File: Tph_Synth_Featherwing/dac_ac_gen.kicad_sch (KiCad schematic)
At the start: 11 parts, among them J3 Conn_01x04, U4 MCP4728

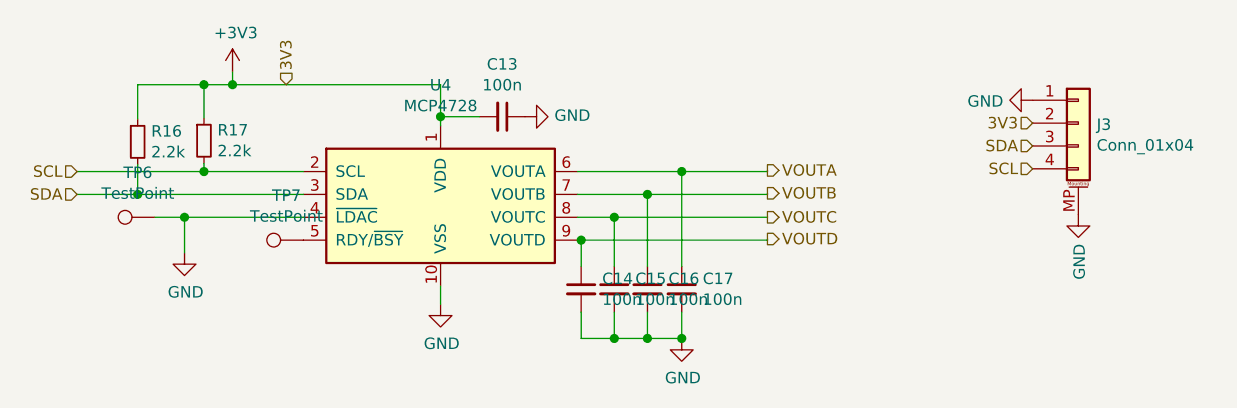
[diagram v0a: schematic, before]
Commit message: Upgrade design to KiCad 10; clear ERC and DRC violations
Co-authored-by: Copilot <223556219+Copilot@users.noreply.github.com>
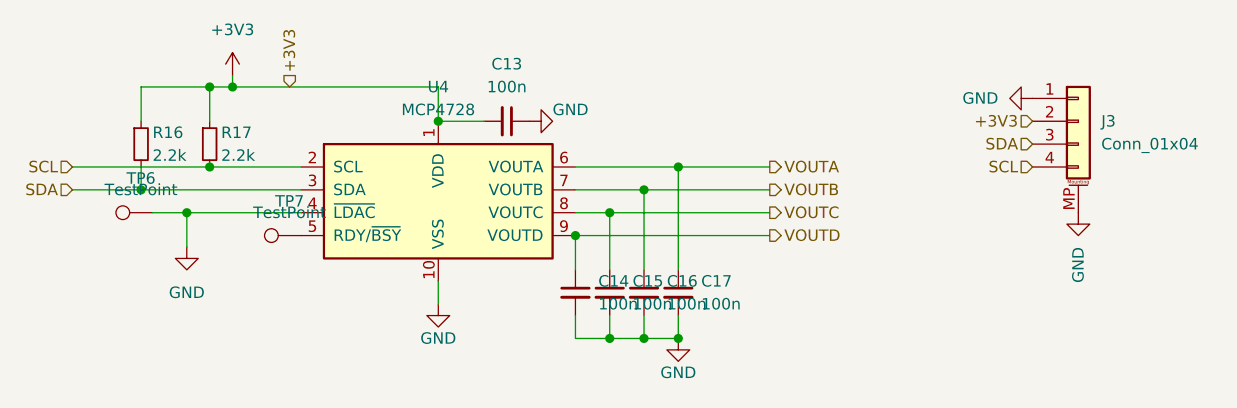
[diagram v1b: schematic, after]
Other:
- moved on the sheet: C13, C14, C15, C16, C17, R17, TP6, TP7, U4

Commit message: Release v0.4 with complete KiCad 10 schematic-PCB parity
Synchronize pad nets, schematic paths, component fields and BOM exclusions while retaining routing and placement. Restore project-local STEP models, fix edge silkscreen using local footprint variants, update revision metadata and improve schematic readability. Include inspected PDF and PCB renders.

Co-authored-by: Copilot <223556219+Copilot@users.noreply.github.com>
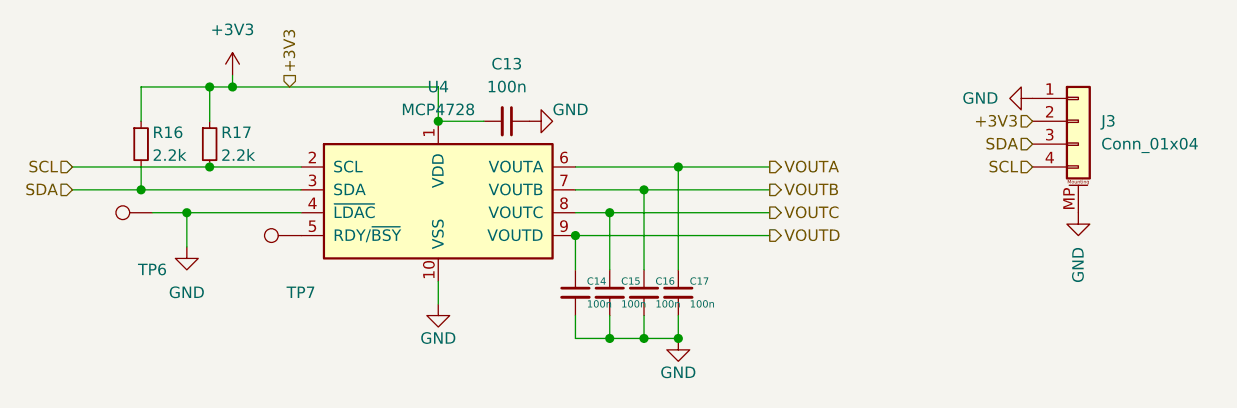
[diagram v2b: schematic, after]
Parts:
- TP6, TP7: now left out of the parts list
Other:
- title: (none) -> 3-Phase Synth FeatherWing
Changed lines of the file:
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@@
 	(generator_version "10.0")
 	(paper "A4")
+	(title_block
+		(title "3-Phase Synth FeatherWing")
+		(date "2026-10-28")
+		(rev "0.4")
+	)
 	(junction
 		(at 71.12 85.09)
@@
 		(body_style 1)
 		(exclude_from_sim no)
-		(in_bom yes)
+		(in_bom no)
 		(on_board yes)
 		(in_pos_files yes)
 		(dnp no)
 		(property "Reference" "TP6"
-			(at 71.12 83.82 90)
+			(at 72.39 93.98 90)
 			(show_name no)
 			(do_not_autoplace no)
@@
 				)
 			)
+			(hide yes)
 		)
 		(property "Footprint" "TestPoint:TestPoint_Pad_D1.0mm"
@@
 		(body_style 1)
 		(exclude_from_sim no)
-		(in_bom yes)
+		(in_bom no)
 		(on_board yes)
 		(in_pos_files yes)
 		(dnp no)
 		(property "Reference" "TP7"
-			(at 87.63 86.36 90)
+			(at 88.9 96.52 90)
 			(show_name no)
 			(do_not_autoplace no)
@@
 				)
 			)
+			(hide yes)
 		)
 		(property "Footprint" "TestPoint:TestPoint_Pad_D1.0mm"
@@
 		(dnp no)
 		(property "Reference" "C14"
-			(at 121.92 95.25 0)
+			(at 120.65 95.25 0)
 			(show_name no)
 			(do_not_autoplace no)
 			(effects
 				(font
-					(size 1.27 1.27)
+					(size 0.8 0.8)
 				)
 				(justify left)
@@
 		)
 		(property "Value" "100n"
-			(at 121.92 97.79 0)
+			(at 120.65 97.79 0)
 			(show_name no)
 			(do_not_autoplace no)
 			(effects
 				(font
-					(size 1.27 1.27)
+					(size 0.8 0.8)
 				)
 				(justify left)
@@
 		(dnp no)
 		(property "Reference" "C15"
-			(at 125.73 95.25 0)
+			(at 124.46 95.25 0)
 			(show_name no)
 			(do_not_autoplace no)
 			(effects
 				(font
-					(size 1.27 1.27)
+					(size 0.8 0.8)
 				)
 				(justify left)
@@
 		)
 		(property "Value" "100n"
-			(at 125.73 97.79 0)
+			(at 124.46 97.79 0)
 			(show_name no)
 			(do_not_autoplace no)
 			(effects
 				(font
-					(size 1.27 1.27)
+					(size 0.8 0.8)
 				)
 				(justify left)
@@
 		(dnp no)
 		(property "Reference" "C16"
-			(at 129.54 95.25 0)
+			(at 128.27 95.25 0)
 			(show_name no)
 			(do_not_autoplace no)
 			(effects
 				(font
-					(size 1.27 1.27)
+					(size 0.8 0.8)
 				)
 				(justify left)
@@
 		)
 		(property "Value" "100n"
-			(at 129.54 97.79 0)
+			(at 128.27 97.79 0)
 			(show_name no)
 			(do_not_autoplace no)
 			(effects
 				(font
-					(size 1.27 1.27)
+					(size 0.8 0.8)
 				)
 				(justify left)
@@
 		(dnp no)
 		(property "Reference" "C17"
-			(at 133.35 95.25 0)
+			(at 132.08 95.25 0)
 			(show_name no)
 			(do_not_autoplace no)
 			(effects
 				(font
-					(size 1.27 1.27)
+					(size 0.8 0.8)
 				)
 				(justify left)
@@
 		)
 		(property "Value" "100n"
-			(at 133.35 97.79 0)
+			(at 132.08 97.79 0)
 			(show_name no)
 			(do_not_autoplace no)
 			(effects
 				(font
-					(size 1.27 1.27)
+					(size 0.8 0.8)
 				)
 				(justify left)
@@
 		(in_pos_files yes)
 		(dnp no)
-		(property "Reference" "#PWR?"
+		(property "Reference" "#PWR0105"
 			(at 163.83 74.93 0)
 			(hide yes)
@@
 			(project "Tph_Synth_Featherwing"
 				(path "/e63e39d7-6ac0-4ffd-8aa3-1841a4541b55/00000000-0000-0000-0000-00005dcbf63f"
-					(reference "#PWR?")
+					(reference "#PWR0105")
 						(unit 1)
 				)
